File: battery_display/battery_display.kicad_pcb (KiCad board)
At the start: 2 copper layers, 100 x 60 mm, 30 parts, among them J1 FH34SRJ-24S-0.5SH_99_, J2 Screw_Terminal_2x2.54, Q1 ZXM61N03F, Q2 ZXM61N03F, SW1 Button-THT - 2-1825910-7, U1 LDO40LPU33RY

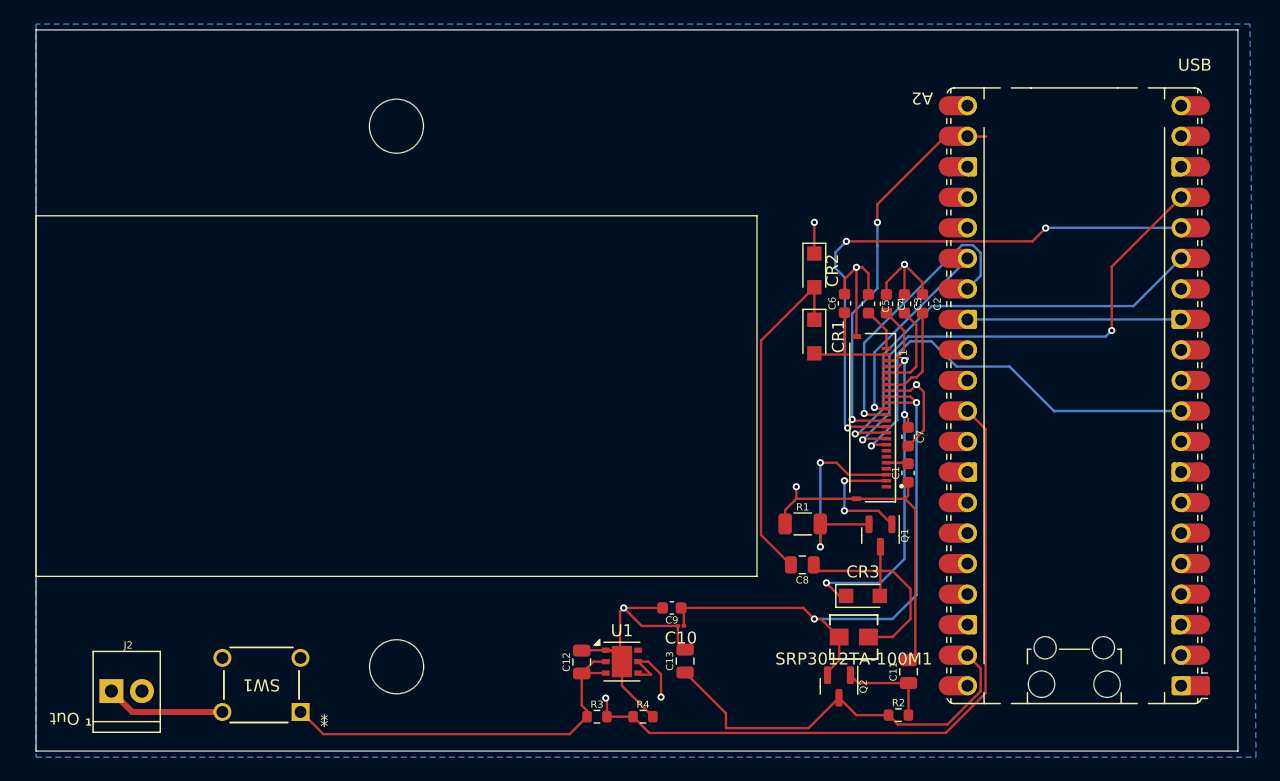
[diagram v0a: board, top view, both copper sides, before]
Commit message: Fixed some warnings
- removed useless via and unconnected wire
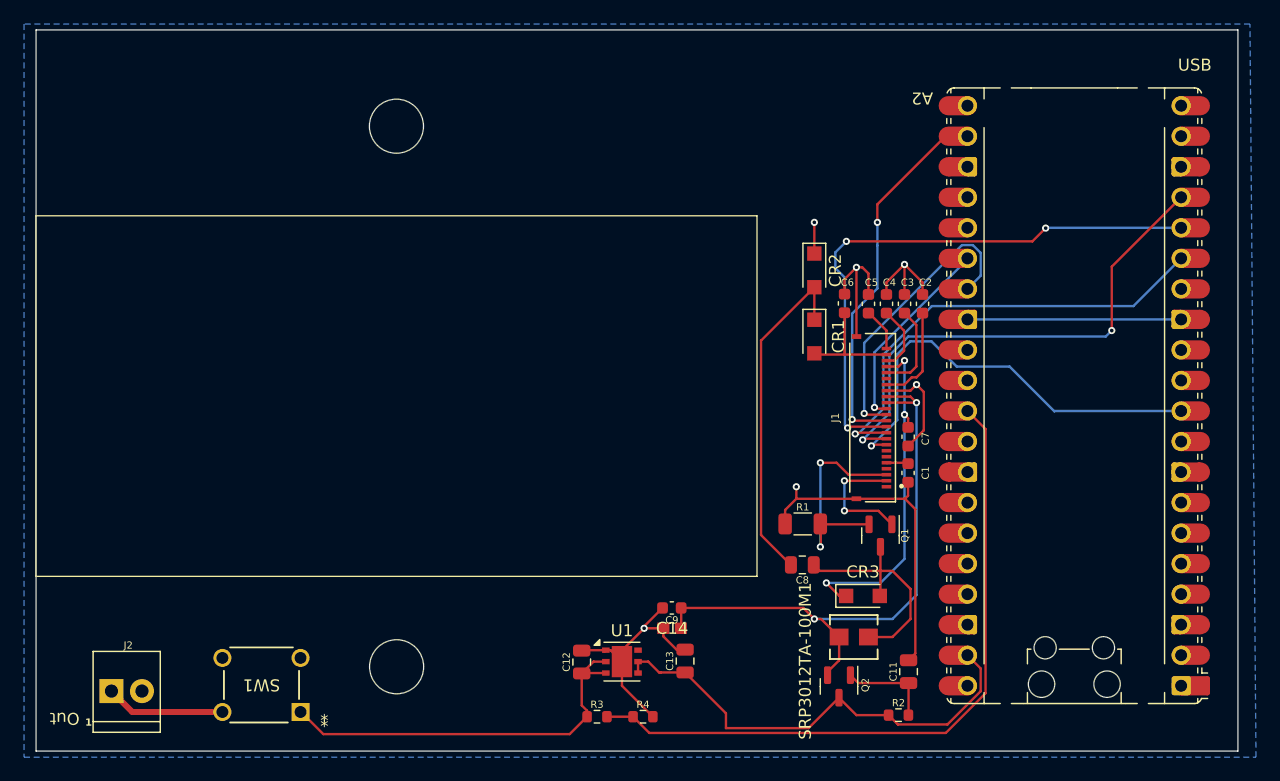
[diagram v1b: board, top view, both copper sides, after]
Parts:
- removed C10: 0u1, Capacitor_SMD:C_01005_0402Metric
- added C14: 100n, rsx_capacitors:CAPC17595_95N_KEM, F.Cu at (207.9, 79.8)
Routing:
- net GND: track 102.0 -> 97.2 mm
- net /panelCS: track 33.1 -> 29.6 mm
- net /3.3V: track 40.7 -> 39.0 mm, vias 1 -> 0
- net /read_voltage: track 59.1 -> 57.5 mm, vias 1 -> 0

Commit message: Fixed Position of drill holes to match E-Stop Drawing
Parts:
- moved H1 10.0 mm to (195.0, 38.0)
- moved H2 10.00 mm to (195.0, 83.0)
- moved R3 2.10 mm to (203.8, 86.9)
- moved C12 2.10 mm to (202.5, 82.3)
- moved C13 2.10 mm to (211.1, 82.2)
- moved C14 2.10 mm to (210.0, 79.5)
- moved C9 2.10 mm to (210.0, 77.8)
- moved R4 2.10 mm to (207.6, 86.9)
- moved U1 2.10 mm to (205.8, 82.3)
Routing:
- net /voltage divider: track 33.8 -> 36.0 mm
- net /3.3V: track 39.0 -> 37.1 mm
- net /Display VDDD: track 50.3 -> 48.3 mm
- net /read_voltage: track 57.5 -> 55.6 mm
